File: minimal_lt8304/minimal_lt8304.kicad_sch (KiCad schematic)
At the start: 27 parts, among them J1 FW-02-03-G-D-085-155, J2 FW-02-03-G-D-085-155, T1 750315836, U1 LT8304IS8E-PBF

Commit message: Update project
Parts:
- added C8: 4.7 nF, capacitor_footprints:C_1210_140_3225Metric, symbol UNITED_CAPACITORS_DATA_BASE:C_C1210C472KFRACAUTO
- added J3, J4: FW-02-03-G-D-085-155, connector_footprints:FW-02-03-G-D-085-155, symbol UNITED_CONNECTORS_DATA_BASE:J_FW-02-03-G-D-085-155
- added MB3, MB4: mouse-bite-midle-50mil-200mil, mouse_bite_footprints:mouse-bite-midle-50mil-200mil, symbol UNITED_MOUSE_BITES_DATA_BASE:mouse-bite-midle-50mil-200mil
- added TP5, TP6, TP7, TP8: TestPoint, test_point_footprints:TestPoint_THTPad_Castelated, symbol UNITED_TEST_POINTS:TestPoint_Castelated
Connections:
- net GND: now also C8.1, J4.1, J4.2, J4.3, J4.4, TP7.1, TP8.1
- net GNDA: now also C8.2, J3.1, J3.2, J3.3, J3.4, TP5.1, TP6.1

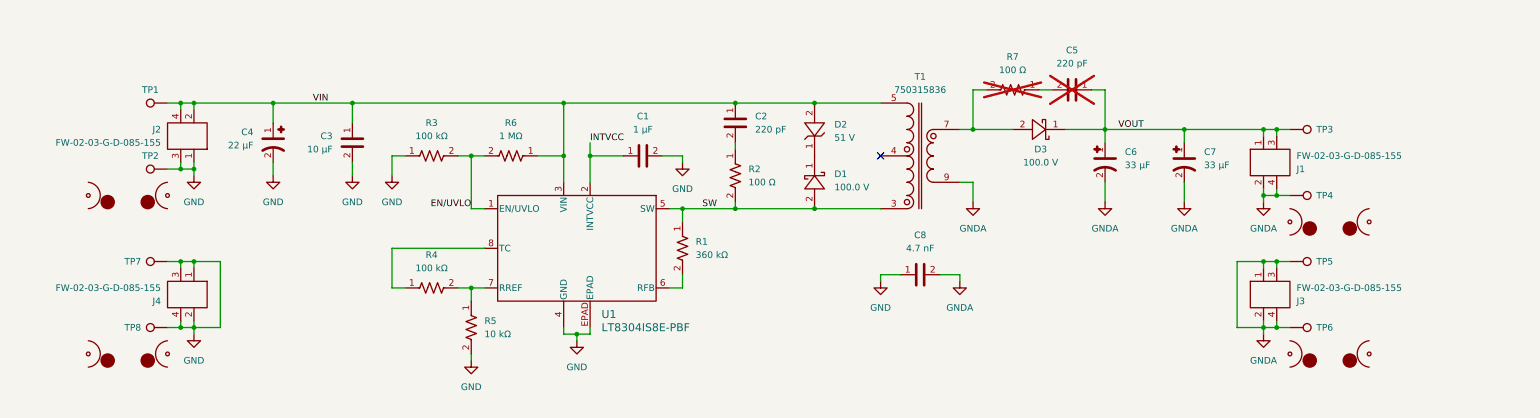
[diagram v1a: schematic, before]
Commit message: Update ibom configuration to include additional component blacklist
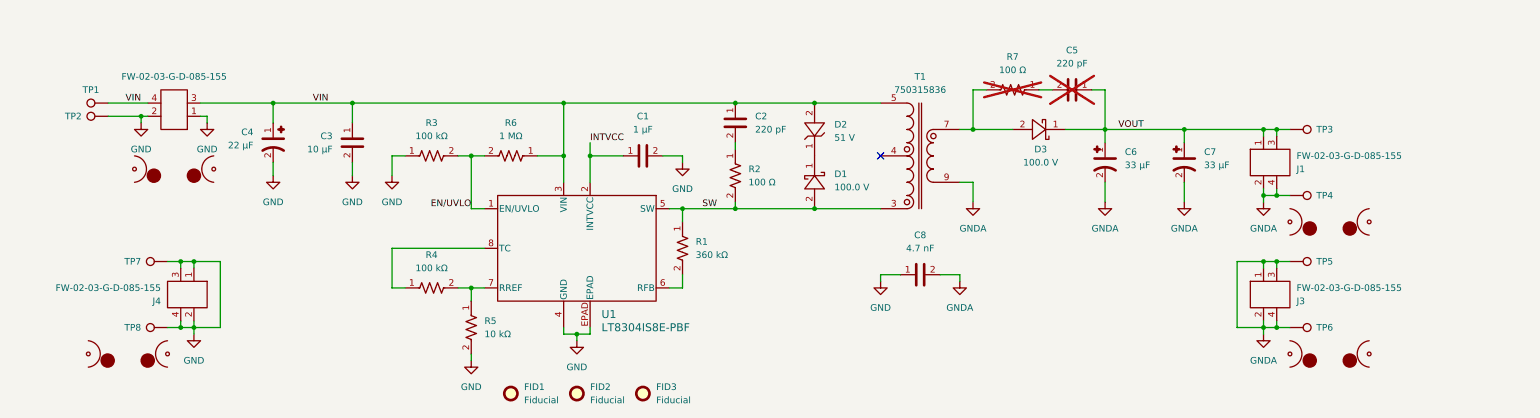
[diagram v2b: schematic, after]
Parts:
- added FID1, FID2, FID3: Fiducial, no_components_footprints:Fiducial_0.5mm_Mask1mm, symbol UNITED_NO_COMPONENTS_DATA_BASE:Fiducial
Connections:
- net GND: now also J2.2; no longer J2.3
- net VIN: now also J2.3; no longer J2.2
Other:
- moved on the sheet: TP1, TP2

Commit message: Switch to KiCad 9
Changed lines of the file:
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@@
 (kicad_sch
-	(version 20231120)
+	(version 20250114)
 	(generator "eeschema")
-	(generator_version "8.0")
+	(generator_version "9.0")
 	(paper "A3")
 	(junction
@@
 		)
 	)
+	(embedded_fonts no)
 )

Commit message: Small project update
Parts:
- added D4: 100.0 V, diode_footprints:SOD123W, symbol UNITED_DIODES_DATA_BASE:D_PMEG10020AELR
- added JP2: SolderJumper_3_Open, solder_jumper_footprints:SolderJumper-3_P1.3mm_Bridged_1_2_RoundedPad1.0x1.5mm_NumberLabels, symbol UNITED_SOLDER_JUMPERS:SolderJumper_3_Bridged_1_2
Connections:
- net VOUT: now also D4.2, JP2.3 (B); no longer J1.1, J1.3, TP3.1
- new net: D4.1, JP2.1 (A)
- new net VOUT_SELECTED: J1.1, J1.3, JP2.2 (C), TP3.1
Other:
- moved on the sheet: J1, TP3, TP4

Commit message: update project
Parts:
- removed J3, J4: FW-02-03-G-D-085-155, connector_footprints:FW-02-03-G-D-085-155, symbol UNITED_CONNECTORS_DATA_BASE:J_FW-02-03-G-D-085-155
- removed MB3, MB4: mouse-bite-midle-50mil-200mil, mouse_bite_footprints:mouse-bite-midle-50mil-200mil, symbol UNITED_MOUSE_BITES_DATA_BASE:mouse-bite-midle-50mil-200mil
- removed TP5, TP6, TP7, TP8: TestPoint, test_point_footprints:TestPoint_THTPad_Castelated, symbol UNITED_TEST_POINTS:TestPoint_Castelated

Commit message: development backup
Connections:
- net GNDA: now also J1.3; no longer J1.2
- net VOUT_SELECTED: now also J1.2; no longer J1.3
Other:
- moved on the sheet: J1, TP3, TP4
